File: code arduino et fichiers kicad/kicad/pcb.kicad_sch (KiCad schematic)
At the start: 46 parts, among them J1 Screw_Terminal_01x04, J2 Screw_Terminal_01x03, U1 LMC6482, U2 LMC6482, U3 LMC6482, U4 LMC6482

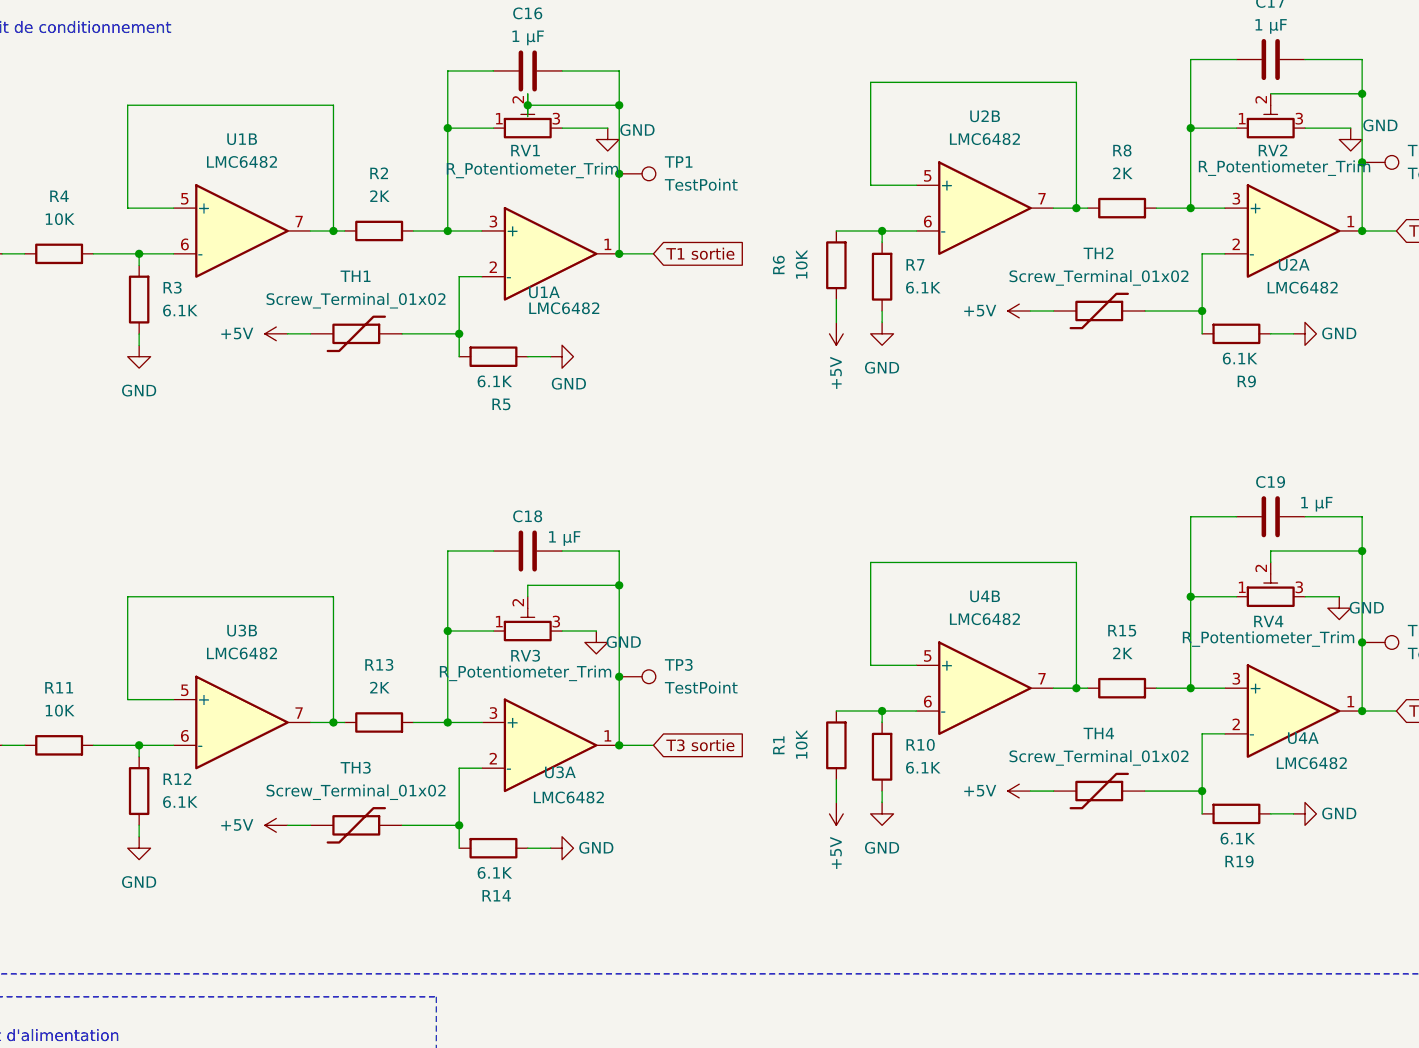
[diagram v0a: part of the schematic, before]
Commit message: Modifs valeur R schematic
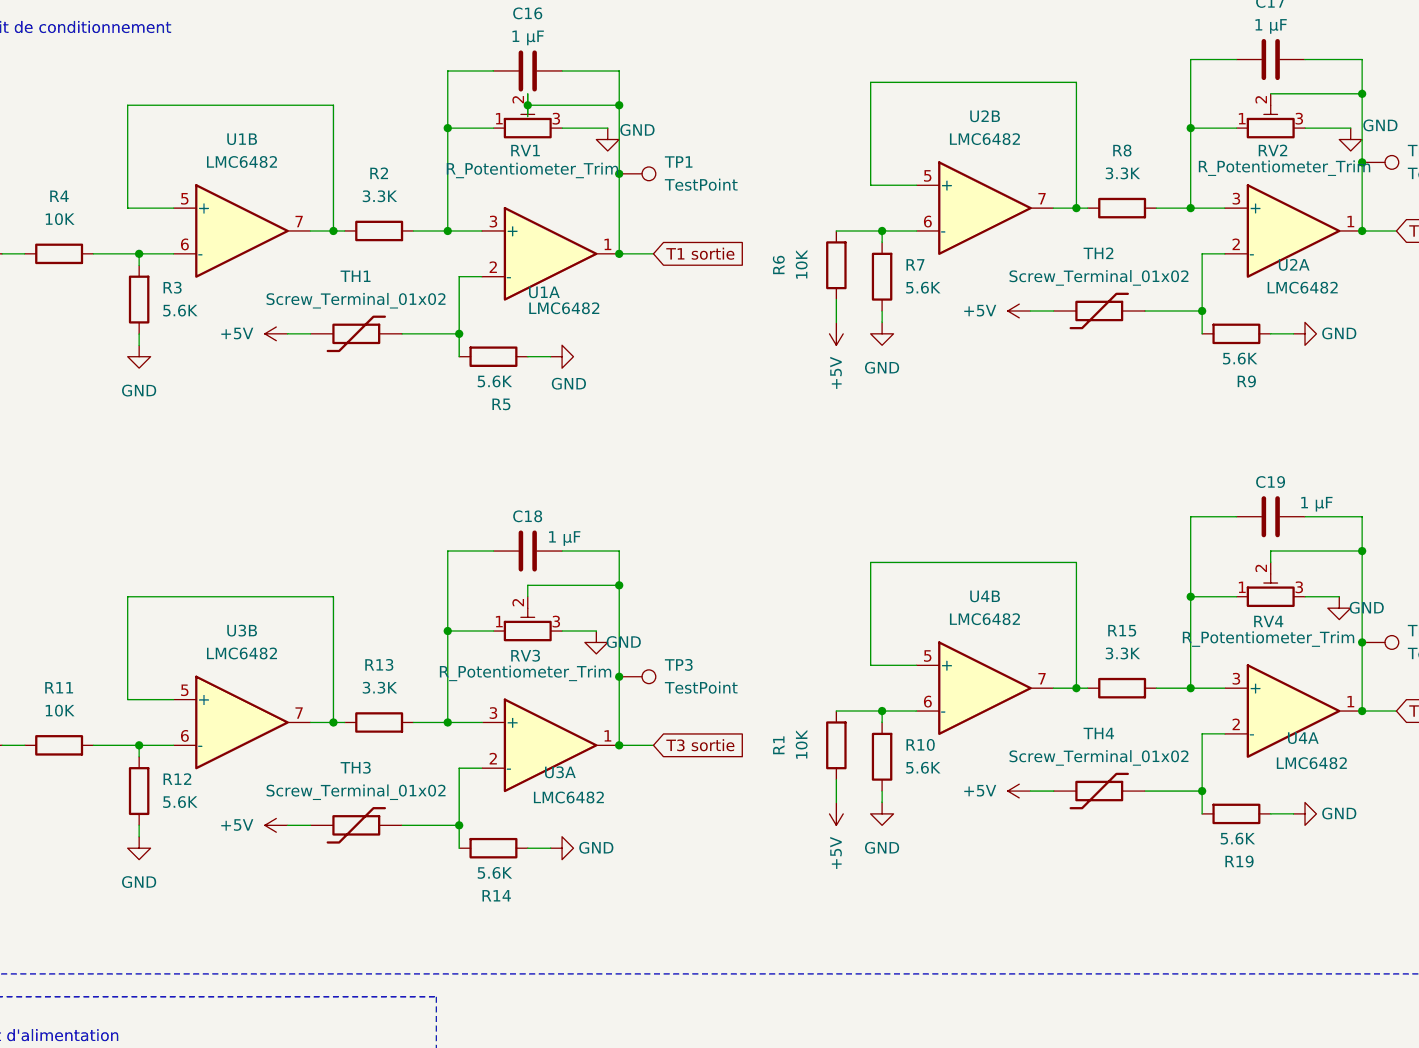
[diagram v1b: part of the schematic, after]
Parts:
- R10, R12, R14, R19, R3, R5, R7, R9: value 6.1K -> 5.6K
- R13, R15, R2, R8: value 2K -> 3.3K
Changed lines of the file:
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@@
 			)
 		)
-		(property "Value" "6.1K"
+		(property "Value" "5.6K"
 			(at 125.73 48.2599 0)
 			(effects
@@
 			)
 		)
-		(property "Value" "6.1K"
+		(property "Value" "5.6K"
 			(at 43.18 105.4099 0)
 			(effects
@@
 			)
 		)
-		(property "Value" "2K"
+		(property "Value" "3.3K"
 			(at 149.86 88.9 90)
 			(effects
@@
 			)
 		)
-		(property "Value" "6.1K"
+		(property "Value" "5.6K"
 			(at 164.846 56.134 90)
 			(effects
@@
 			)
 		)
-		(property "Value" "6.1K"
+		(property "Value" "5.6K"
 			(at 125.73 101.5999 0)
 			(effects
@@
 			)
 		)
-		(property "Value" "2K"
+		(property "Value" "3.3K"
 			(at 67.31 92.71 90)
 			(effects
@@
 			)
 		)
-		(property "Value" "2K"
+		(property "Value" "3.3K"
 			(at 67.31 38.1 90)
 			(effects
@@
 			)
 		)
-		(property "Value" "6.1K"
+		(property "Value" "5.6K"
 			(at 82.042 58.674 90)
 			(effects
@@
 			)
 		)
-		(property "Value" "6.1K"
+		(property "Value" "5.6K"
 			(at 164.592 109.474 90)
 			(effects
@@
 			)
 		)
-		(property "Value" "6.1K"
+		(property "Value" "5.6K"
 			(at 82.042 113.284 90)
 			(effects
@@
 			)
 		)
-		(property "Value" "6.1K"
+		(property "Value" "5.6K"
 			(at 43.18 50.7999 0)
 			(effects
@@
 		(on_board yes)
 		(dnp no)
-		(fields_autoplaced yes)
 		(property "Reference" "TP2"
 			(at 181.61 33.0199 90)
@@
 			)
 		)
-		(property "Value" "2K"
+		(property "Value" "3.3K"
 			(at 149.86 35.56 90)
 			(effects

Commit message: esti de kicad
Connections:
- net at C18.1, R13.2, RV3.1: now also U3.2 (-); no longer U3.3 (+)
- net at R6.2, R7.2: now also U2.5 (+); no longer U2.6 (-)
- net at R11.2, R12.2: now also U3.5 (+); no longer U3.6 (-)
- net at C19.1, R15.2, RV4.1: now also U4.2 (-); no longer U4.3 (+)
- net at R15.1, U4.7: now also U4.6 (-); no longer U4.5 (+)
- net at R9.2, TH2.1: now also U2.3 (+); no longer U2.2 (-)
- net at C17.1, R8.2, RV2.1: now also U2.2 (-); no longer U2.3 (+)
- net at R1.2, R10.2: now also U4.5 (+); no longer U4.6 (-)
- net at R14.2, TH3.1: now also U3.3 (+); no longer U3.2 (-)
- net at R8.1, U2.7: now also U2.6 (-); no longer U2.5 (+)
- net at R19.2, TH4.1: now also U4.3 (+); no longer U4.2 (-)
- net at R5.2, TH1.1: now also U1.3 (+); no longer U1.2 (-)
- net at C16.1, R2.2, RV1.1: now also U1.2 (-); no longer U1.3 (+)
- net at R13.1, U3.7: now also U3.6 (-); no longer U3.5 (+)
- net at R2.1, U1.7: now also U1.6 (-); no longer U1.5 (+)
- net at R3.2, R4.2: now also U1.5 (+); no longer U1.6 (-)
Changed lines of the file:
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@@
 		(lib_id "Amplifier_Operational:LMC6482")
 		(at 168.91 41.91 0)
+		(mirror x)
 		(unit 1)
 		(exclude_from_sim no)
@@
 		(dnp no)
 		(property "Reference" "U2"
-			(at 168.91 45.72 0)
+			(at 168.91 38.1 0)
 			(effects
 				(font
@@
 		)
 		(property "Value" "LMC6482"
-			(at 169.926 48.26 0)
+			(at 169.926 35.56 0)
 			(effects
 				(font
@@
 		(lib_id "Amplifier_Operational:LMC6482")
 		(at 86.36 99.06 0)
+		(mirror x)
 		(unit 1)
 		(exclude_from_sim no)
@@
 		(dnp no)
 		(property "Reference" "U3"
-			(at 87.376 102.108 0)
+			(at 87.376 96.012 0)
 			(effects
 				(font
@@
 		)
 		(property "Value" "LMC6482"
-			(at 88.392 104.902 0)
+			(at 88.392 93.218 0)
 			(effects
 				(font
@@
 		(lib_id "Amplifier_Operational:LMC6482")
 		(at 134.62 39.37 0)
+		(mirror x)
 		(unit 2)
 		(exclude_from_sim no)
@@
 		(on_board yes)
 		(dnp no)
-		(fields_autoplaced yes)
 		(property "Reference" "U2"
-			(at 134.62 29.21 0)
+			(at 134.62 49.53 0)
 			(effects
 				(font
@@
 		)
 		(property "Value" "LMC6482"
-			(at 134.62 31.75 0)
+			(at 134.62 46.99 0)
 			(effects
 				(font
@@
 		(lib_id "Amplifier_Operational:LMC6482")
 		(at 168.91 95.25 0)
+		(mirror x)
 		(unit 1)
 		(exclude_from_sim no)
@@
 		(dnp no)
 		(property "Reference" "U4"
-			(at 169.926 98.298 0)
+			(at 169.926 92.202 0)
 			(effects
 				(font
@@
 		)
 		(property "Value" "LMC6482"
-			(at 170.942 101.092 0)
+			(at 170.942 89.408 0)
 			(effects
 				(font
@@
 		(lib_id "Amplifier_Operational:LMC6482")
 		(at 86.36 44.45 0)
+		(mirror x)
 		(unit 1)
 		(exclude_from_sim no)
@@
 		(dnp no)
 		(property "Reference" "U1"
-			(at 85.598 48.768 0)
+			(at 85.598 40.132 0)
 			(effects
 				(font
@@
 		)
 		(property "Value" "LMC6482"
-			(at 87.884 50.546 0)
+			(at 87.884 38.354 0)
 			(effects
 				(font
@@
 		(lib_id "Amplifier_Operational:LMC6482")
 		(at 52.07 41.91 0)
+		(mirror x)
 		(unit 2)
 		(exclude_from_sim no)
@@
 		(on_board yes)
 		(dnp no)
-		(fields_autoplaced yes)
 		(property "Reference" "U1"
-			(at 52.07 31.75 0)
+			(at 52.07 52.07 0)
 			(effects
 				(font
@@
 		)
 		(property "Value" "LMC6482"
-			(at 52.07 34.29 0)
+			(at 52.07 49.53 0)
 			(effects
 				(font
@@
 		(lib_id "Amplifier_Operational:LMC6482")
 		(at 52.07 96.52 0)
+		(mirror x)
 		(unit 2)
 		(exclude_from_sim no)
@@
 		(on_board yes)
 		(dnp no)
-		(fields_autoplaced yes)
 		(property "Reference" "U3"
-			(at 52.07 86.36 0)
+			(at 52.07 106.68 0)
 			(effects
 				(font
@@
 		)
 		(property "Value" "LMC6482"
-			(at 52.07 88.9 0)
+			(at 52.07 104.14 0)
 			(effects
 				(font
@@
 		(lib_id "Amplifier_Operational:LMC6482")
 		(at 134.62 92.71 0)
+		(mirror x)
 		(unit 2)
 		(exclude_from_sim no)
@@
 		(on_board yes)
 		(dnp no)
-		(fields_autoplaced yes)
 		(property "Reference" "U4"
-			(at 134.62 82.55 0)
+			(at 134.62 102.87 0)
 			(effects
 				(font
@@
 		)
 		(property "Value" "LMC6482"
-			(at 134.62 85.09 0)
-			(effects
-				(font
+			(at 134.62 100.33 0)
+			(effects
+				(font

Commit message: PCB V2
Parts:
- removed J1: Screw_Terminal_01x04, Connector_JST:JST_XH_B4B-XH-A_1x04_P2.50mm_Vertical, symbol Connector:Screw_Terminal_01x04
- removed J2: Screw_Terminal_01x03, Connector_JST:JST_XH_B3B-XH-A_1x03_P2.50mm_Vertical, symbol Connector:Screw_Terminal_01x03
- removed U1, U2, U3, U4: LMC6482, ampli op:LMC6482_SMT, symbol Amplifier_Operational:LMC6482
- added J1: MTA_02, ampli op:MTA_CONN2_640445-2, symbol New_Library:MTA_02
- added J2: MTA_04, ampli op:MTA_CONN4_640445-4, symbol New_Library:MTA_04
- added U1, U2, U3, U4: LMC6482IMX_NOPB, ampli op:LMC6482_SMT, symbol New_Library:LMC6482IMX_NOPB
- TH1, TH2, TH3, TH4: footprint Connector_JST:JST_XH_B2B-XH-A_1x02_P2.50mm_Vertical -> ampli op:MTA_CONN2_640445-2
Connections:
- net +5V: now also R1.2, U1.8 (V+), U2.8 (V+), U3.8 (V+), U4.8 (V+); no longer R1.1
- net +5V (Ali seulement): now also J1.2, J2.4
- net +AREF: now also pwm1.3 (Pin_3); no longer pwm1.8 (Pin_8)
- net D0/RX0: now also pwm2.8 (Pin_8); no longer pwm2.1 (Pin_1)
- net D10: now also pwm1.8 (Pin_8); no longer pwm1.3 (Pin_3)
- net D12: now also pwm1.6 (Pin_6); no longer pwm1.5 (Pin_5)
- net D13: now also pwm1.5 (Pin_5); no longer pwm1.6 (Pin_6)
- net D1/TX0: now also pwm2.7 (Pin_7); no longer pwm2.2 (Pin_2)
- net D2: now also pwm2.6 (Pin_6); no longer pwm2.3 (Pin_3)
- net D3: now also pwm2.5 (Pin_5); no longer pwm2.4 (Pin_4)
- net D4: now also pwm2.4 (Pin_4); no longer pwm2.5 (Pin_5)
- net D6: now also pwm2.2 (Pin_2); no longer pwm2.7 (Pin_7)
- net D7: now also pwm2.1 (Pin_1); no longer pwm2.8 (Pin_8)
- net D8: now also pwm1.10 (Pin_10); no longer pwm1.1 (Pin_1)
- net D9: now also pwm1.9 (Pin_9); no longer pwm1.2 (Pin_2)
- net GND: now also R10.2, R14.2, R19.2, R9.2, pwm1.4 (Pin_4), J1.1, J2.3, U1.4 (V-), U2.4 (V-), U3.4 (V-), U4.4 (V-); no longer R10.1, R14.1, R19.1, R9.1, pwm1.7 (Pin_7)
- net SCL: now also pwm1.1 (Pin_1); no longer pwm1.10 (Pin_10)
- net SDA: now also pwm1.2 (Pin_2); no longer pwm1.9 (Pin_9)
- net T1 sortie: now also U1.7 (OUTB)
- net T2 sortie: now also U2.7 (OUTB)
- net T3 sortie: now also U3.7 (OUTB)
- net T4 sortie: now also U4.7 (OUTB)
- net pwmdroite: now also pwm2.3 (Pin_3), J2.1; no longer pwm2.6 (Pin_6)
- net pwmgauche: now also pwm1.7 (Pin_7), J2.2; no longer pwm1.4 (Pin_4)
- net at C18.1, RV3.1: now also R13.1, U3.6 (NEGB); no longer R13.2
- net at R6.2, R7.2: now also U2.3 (POSA)
- net at R11.2, R12.2: now also U3.3 (POSA)
- net at C19.1, RV4.1: now also R15.1, U4.6 (NEGB); no longer R15.2
- net at C17.1, RV2.1: now also R8.1, U2.6 (NEGB); no longer R8.2
- net at TH2.1: now also R9.1, U2.5 (POSB); no longer R9.2
- net at TH3.1: now also R14.1, U3.5 (POSB); no longer R14.2
- net at TH4.1: now also R19.1, U4.5 (POSB); no longer R19.2
- net at C16.1, RV1.1: now also R2.1, U1.6 (NEGB); no longer R2.2
- net at R5.2, TH1.1: now also U1.5 (POSB)
- net at R3.2, R4.2: now also U1.3 (POSA)
- new net: R15.2, U4.1 (OUTA), U4.2 (NEGA)
- new net: R1.1, R10.1, U4.3 (POSA)
- new net: R13.2, U3.1 (OUTA), U3.2 (NEGA)
- new net: R8.2, U2.1 (OUTA), U2.2 (NEGA)
- new net: R2.2, U1.1 (OUTA), U1.2 (NEGA)
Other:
- moved on the sheet: C16, C17, C18, C19, D4, R1, R10, R11, R12, R13, R14, R15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

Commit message: Gerber files exportés, on commande?
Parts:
- renumbered C16 to C1, C17 to C2, C18 to C3, C19 to C4, D4 to D1
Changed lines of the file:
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@@
 		(on_board yes)
 		(dnp no)
-		(property "Reference" "C18"
+		(property "Reference" "C3"
 			(at 35.56 93.98 90)
 			(effects
@@
 			(project "pcb"
 				(path "/08655c7e-db3e-4a36-827c-446c5903f8cb"
-					(reference "C18")
+					(reference "C3")
 					(unit 1)
 				)
@@
 		(dnp no)
 		(fields_autoplaced yes)
-		(property "Reference" "D4"
+		(property "Reference" "D1"
 			(at 152.3365 176.53 0)
 			(effects
@@
 			(project ""
 				(path "/08655c7e-db3e-4a36-827c-446c5903f8cb"
-					(reference "D4")
+					(reference "D1")
 					(unit 1)
 				)
@@
 		(on_board yes)
 		(dnp no)
-		(property "Reference" "C19"
+		(property "Reference" "C4"
 			(at 125.73 95.25 90)
 			(effects
@@
 			(project "pcb"
 				(path "/08655c7e-db3e-4a36-827c-446c5903f8cb"
-					(reference "C19")
+					(reference "C4")
 					(unit 1)
 				)
@@
 		(on_board yes)
 		(dnp no)
-		(property "Reference" "C17"
+		(property "Reference" "C2"
 			(at 127 19.05 90)
 			(effects
@@
 			(project "pcb"
 				(path "/08655c7e-db3e-4a36-827c-446c5903f8cb"
-					(reference "C17")
+					(reference "C2")
 					(unit 1)
 				)
@@
 		(on_board yes)
 		(dnp no)
-		(property "Reference" "C16"
+		(property "Reference" "C1"
 			(at 35.56 21.59 90)
 			(effects
@@
 			(project ""
 				(path "/08655c7e-db3e-4a36-827c-446c5903f8cb"
-					(reference "C16")
+					(reference "C1")
 					(unit 1)
 				)
